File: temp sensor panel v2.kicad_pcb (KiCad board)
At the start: 2 copper layers, 48.2 x 24.9 mm, 51 parts, among them IC1 ESP32-C3-MINI-1, J1 USB_C_Receptacle_USB2.0, J2 Conn_01x02_Male, J3 Conn_01x06_Male, J4 USB_B_Micro, J5 Conn_01x02_Male, J6 Conn_01x02_Male, Q1 BC847BDW1, SW1 SW_Push_Right_Angle, SW2 SW_Push_Right_Angle, U1 SHTC3, U2 TLV62569DBV, U3 BME280, U4 Si7020-A20, U5 SN65220

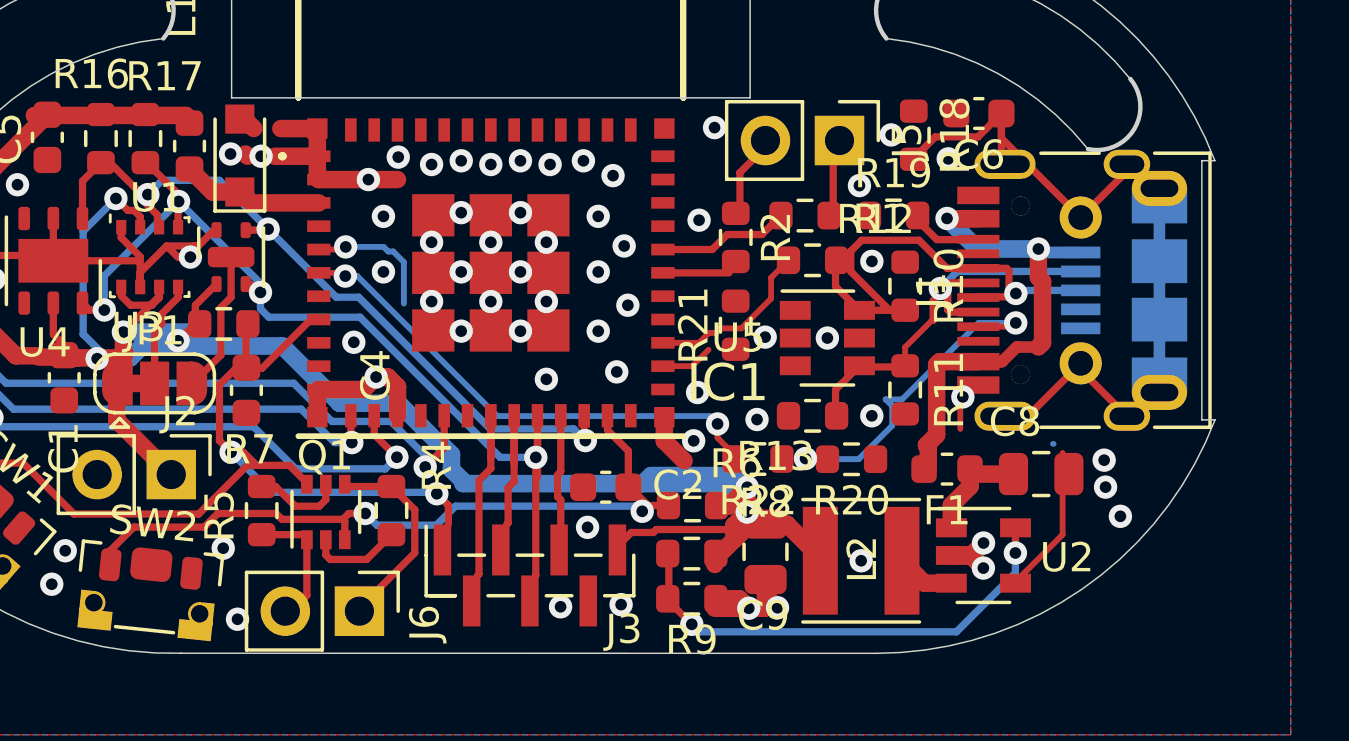
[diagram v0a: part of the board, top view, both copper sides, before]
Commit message: added fuse and some layout changes
Signed-off-by: lokimetasmith <lokimail@gmail.com>
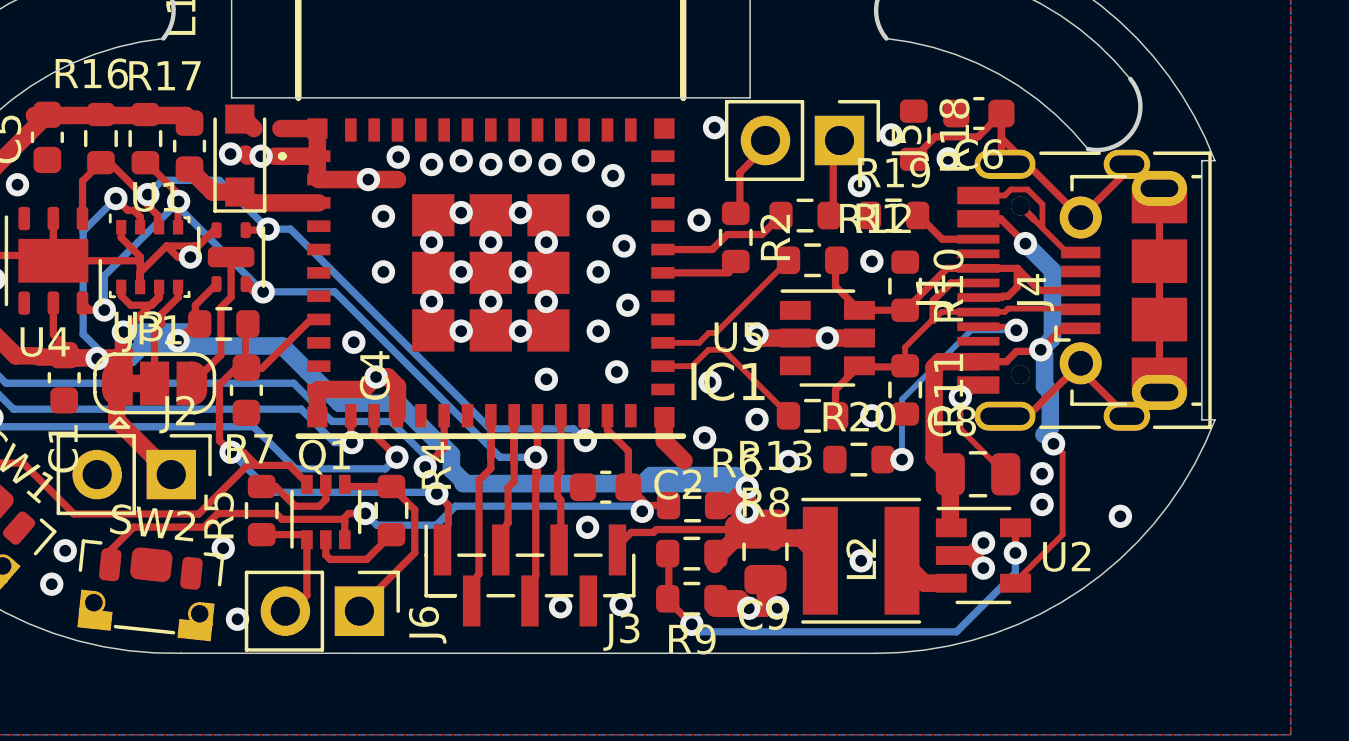
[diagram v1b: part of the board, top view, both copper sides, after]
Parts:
- removed F1: 6V 0.5A, Fuse:Fuse_0603_1608Metric
- removed R21, R22: 5.1k, Resistor_SMD:R_0603_1608Metric
- J4: moved to F.Cu
- moved C8 2.17 mm to (157.0, 99.0)
- moved R20 0.25 mm to (153.0, 98.5), turned to 0 degrees
- turned J4 to 90 degrees
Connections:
- net /CC1 renamed Net-(J1-PadA5)
- net /CC2 renamed Net-(J1-PadB5)
- IC1 pad 5: /I37_pico -> (no net)
- IC1 pad 6: /I38_pico -> (no net)
- J1 pad : (no net) -> GND
- J1 pad A4: /V_USB -> +5V
- J1 pad A9: /V_USB -> +5V
- J1 pad B4: /V_USB -> +5V
- J1 pad B9: /V_USB -> +5V
- J4 pad 1: /V_USB -> +5V
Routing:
- net +5V: track 9.04 -> 26.7 mm, vias 0 -> 3
- net /I38_pico: track 17.3 -> 0.00 mm, vias 2 -> 0
- net /V_USB: track 17.1 -> 0.00 mm, vias 2 -> 0
- net GND: track 45.5 -> 57.4 mm, vias 67 -> 69
- net /D+: track 17.3 -> 12.7 mm, vias 1 -> 0
- net /I37_pico: track 4.59 -> 0.00 mm, vias 1 -> 0
- net /IO20_pico: track 1.80 -> 5.52 mm
- net Net-(J1-PadA5): track 11.2 -> 8.97 mm, vias 3 -> 2
- net /D-: track 15.2 -> 13.4 mm, vias 1 -> 0

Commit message: initial work on gerber files, there's an error where arches aren't rendered correctly
Signed-off-by: lokimetasmith <lokimail@gmail.com>
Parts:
- removed the C8 at (157.0, 99.0)
- removed the JP1 at (128.8, 95.8)
- removed the R10 at (154.5, 92.5)
- removed the R11 at (154.5, 96.1)
- removed the R12 at (151.4, 91.6)
- removed the R13 at (151.4, 97.0)
- removed the R20 at (153.0, 98.5)
- removed the U5 at (151.9, 94.3)
- added C1: 0.1u, Capacitor_SMD:C_0603_1608Metric, F.Cu at (33.6, 182.6)
- added C1: 0.1u, Capacitor_SMD:C_0603_1608Metric, F.Cu at (63.2, 148.3)
- added C1: 0.1u, Capacitor_SMD:C_0603_1608Metric, F.Cu at (120.8, 148.3)
- added C1: 0.1u, Capacitor_SMD:C_0603_1608Metric, F.Cu at (91.2, 182.6)
- added C2: 0.1u, Capacitor_SMD:C_0603_1608Metric, F.Cu at (44.7, 144.6)
- added C2: 0.1u, Capacitor_SMD:C_0603_1608Metric, F.Cu at (52.2, 186.4)
- added C2: 0.1u, Capacitor_SMD:C_0603_1608Metric, F.Cu at (102.2, 144.6)
- added C2: 0.1u, Capacitor_SMD:C_0603_1608Metric, F.Cu at (109.8, 186.4)
- added C3: 10u, Capacitor_SMD:C_0805_2012Metric, F.Cu at (30.4, 177.5)
- added C3: 10u, Capacitor_SMD:C_0805_2012Metric, F.Cu at (66.5, 153.4)
- added C3: 10u, Capacitor_SMD:C_0805_2012Metric, F.Cu at (124.0, 153.4)
- added C3: 10u, Capacitor_SMD:C_0805_2012Metric, F.Cu at (88.0, 177.5)
- added C4: 0.1u, Capacitor_SMD:C_0603_1608Metric, F.Cu at (57.0, 147.9)
- added C4: 0.1u, Capacitor_SMD:C_0603_1608Metric, F.Cu at (39.9, 183.1)
- added C4: 0.1u, Capacitor_SMD:C_0603_1608Metric, F.Cu at (114.5, 147.9)
- added C4: 0.1u, Capacitor_SMD:C_0603_1608Metric, F.Cu at (97.5, 183.1)
- added C5: 0.1u, Capacitor_SMD:C_0603_1608Metric, F.Cu at (63.8, 156.6)
- added C5: 0.1u, Capacitor_SMD:C_0603_1608Metric, F.Cu at (33.1, 174.4)
- added C5: 0.1u, Capacitor_SMD:C_0603_1608Metric, F.Cu at (121.4, 156.6)
- added C5: 0.1u, Capacitor_SMD:C_0603_1608Metric, F.Cu at (90.6, 174.4)
- added C6: 0.01u, Capacitor_SMD:C_0603_1608Metric, F.Cu at (31.9, 157.4)
- added C6: 0.01u, Capacitor_SMD:C_0603_1608Metric, F.Cu at (65.0, 173.6)
- added C6: 0.01u, Capacitor_SMD:C_0603_1608Metric, F.Cu at (89.4, 157.4)
- added C6: 0.01u, Capacitor_SMD:C_0603_1608Metric, F.Cu at (122.6, 173.6)
- added C8: 4.7u, Capacitor_SMD:C_0805_2012Metric, F.Cu at (29.7, 145.0)
- added C8: 4.7u, Capacitor_SMD:C_0805_2012Metric, F.Cu at (67.1, 185.9)
- added C8: 4.7u, Capacitor_SMD:C_0805_2012Metric, F.Cu at (87.3, 145.0)
- added C8: 4.7u, Capacitor_SMD:C_0805_2012Metric, F.Cu at (124.7, 185.9)
- added C8: 4.7u, Capacitor_SMD:C_0805_2012Metric, F.Cu at (159.2, 98.9)
- added C9: 10u, Capacitor_SMD:C_0805_2012Metric, F.Cu at (57.7, 188.6)
- added C9: 10u, Capacitor_SMD:C_0805_2012Metric, F.Cu at (39.2, 142.3)
- added C9: 10u, Capacitor_SMD:C_0805_2012Metric, F.Cu at (96.7, 142.3)
- added C9: 10u, Capacitor_SMD:C_0805_2012Metric, F.Cu at (115.3, 188.6)
- added D1: 3.3v_TVS, Diode_SMD:D_SOD-323_HandSoldering, F.Cu at (39.7, 175.0)
- added D1: 3.3v_TVS, Diode_SMD:D_SOD-323_HandSoldering, F.Cu at (57.2, 155.9)
- added D1: 3.3v_TVS, Diode_SMD:D_SOD-323_HandSoldering, F.Cu at (114.8, 155.9)
- added D1: 3.3v_TVS, Diode_SMD:D_SOD-323_HandSoldering, F.Cu at (97.2, 175.0)
- added D2: QLS6A, LED_SMD:LED_Cree-PLCC6_4.7x1.5mm, F.Cu at (26.2, 179.6)
- added D2: QLS6A, LED_SMD:LED_Cree-PLCC6_4.7x1.5mm, F.Cu at (70.7, 151.3)
- added D2: QLS6A, LED_SMD:LED_Cree-PLCC6_4.7x1.5mm, F.Cu at (128.3, 151.3)
- added D2: QLS6A, LED_SMD:LED_Cree-PLCC6_4.7x1.5mm, F.Cu at (83.7, 179.6)
- added F1: 6V 0.5A, Fuse:Fuse_0603_1608Metric, F.Cu at (63.9, 185.8)
- added F1: 6V 0.5A, Fuse:Fuse_0603_1608Metric, F.Cu at (33.0, 145.2)
- added F1: 6V 0.5A, Fuse:Fuse_0603_1608Metric, F.Cu at (90.5, 145.2)
- added F1: 6V 0.5A, Fuse:Fuse_0603_1608Metric, F.Cu at (121.5, 185.8)
- added F1: 6V 0.5A, Fuse:Fuse_0603_1608Metric, F.Cu at (156.0, 98.8)
- added IC1: ESP32-C3-MINI-1, Twig:ESP32C3MINI1, F.Cu at (48.6, 154.6)
- added IC1: ESP32-C3-MINI-1, Twig:ESP32C3MINI1, F.Cu at (48.3, 176.3)
- added IC1: ESP32-C3-MINI-1, Twig:ESP32C3MINI1, F.Cu at (106.2, 154.6)
- added IC1: ESP32-C3-MINI-1, Twig:ESP32C3MINI1, F.Cu at (105.8, 176.3)
- added J1: USB_C_Receptacle_USB2.0, Connector_USB:USB_C_Receptacle_HRO_TYPE-C-31-M-12, F.Cu at (27.8, 151.3)
- added J1: USB_C_Receptacle_USB2.0, Connector_USB:USB_C_Receptacle_HRO_TYPE-C-31-M-12, F.Cu at (69.0, 179.6)
- added J1: USB_C_Receptacle_USB2.0, Connector_USB:USB_C_Receptacle_HRO_TYPE-C-31-M-12, F.Cu at (85.4, 151.3)
- added J1: USB_C_Receptacle_USB2.0, Connector_USB:USB_C_Receptacle_HRO_TYPE-C-31-M-12, F.Cu at (126.6, 179.6)
- added J2: Conn_01x02_Male, Connector_PinHeader_2.54mm:PinHeader_1x02_P2.54mm_Vertical, F.Cu at (37.3, 186.0)
- added J2: Conn_01x02_Male, Connector_PinHeader_2.54mm:PinHeader_1x02_P2.54mm_Vertical, F.Cu at (59.6, 145.0)
- added J2: Conn_01x02_Male, Connector_PinHeader_2.54mm:PinHeader_1x02_P2.54mm_Vertical, F.Cu at (117.1, 145.0)
- added J2: Conn_01x02_Male, Connector_PinHeader_2.54mm:PinHeader_1x02_P2.54mm_Vertical, F.Cu at (94.9, 186.0)
- added J3: Conn_01x06_Male, Connector_PinHeader_1.00mm:PinHeader_1x07_P1.00mm_Vertical_SMD_Pin1Right, F.Cu at (47.3, 141.5)
- added J3: Conn_01x06_Male, Connector_PinHeader_1.00mm:PinHeader_1x07_P1.00mm_Vertical_SMD_Pin1Right, F.Cu at (49.6, 189.4)
- added J3: Conn_01x06_Male, Connector_PinHeader_1.00mm:PinHeader_1x07_P1.00mm_Vertical_SMD_Pin1Right, F.Cu at (104.8, 141.5)
- added J3: Conn_01x06_Male, Connector_PinHeader_1.00mm:PinHeader_1x07_P1.00mm_Vertical_SMD_Pin1Right, F.Cu at (107.2, 189.4)
- added J4: USB_B_Micro, Connector_USB:USB_Micro-B_Molex-105017-0001, B.Cu at (26.9, 151.3)
- added J4: USB_B_Micro, Connector_USB:USB_Micro-B_Molex-105017-0001, B.Cu at (70.0, 179.6)
- added J4: USB_B_Micro, Connector_USB:USB_Micro-B_Molex-105017-0001, B.Cu at (84.5, 151.3)
- added J4: USB_B_Micro, Connector_USB:USB_Micro-B_Molex-105017-0001, B.Cu at (127.5, 179.6)
- added J5: Conn_01x02_Male, Connector_PinHeader_2.54mm:PinHeader_1x02_P2.54mm_Vertical, F.Cu at (36.6, 156.4)
- added J5: Conn_01x02_Male, Connector_PinHeader_2.54mm:PinHeader_1x02_P2.54mm_Vertical, F.Cu at (60.2, 174.5)
- added J5: Conn_01x02_Male, Connector_PinHeader_2.54mm:PinHeader_1x02_P2.54mm_Vertical, F.Cu at (94.2, 156.4)
- added J5: Conn_01x02_Male, Connector_PinHeader_2.54mm:PinHeader_1x02_P2.54mm_Vertical, F.Cu at (117.8, 174.5)
- added J6: Conn_01x02_Male, Connector_PinHeader_2.54mm:PinHeader_1x02_P2.54mm_Vertical, F.Cu at (53.1, 140.3)
- added J6: Conn_01x02_Male, Connector_PinHeader_2.54mm:PinHeader_1x02_P2.54mm_Vertical, F.Cu at (43.8, 190.6)
- added J6: Conn_01x02_Male, Connector_PinHeader_2.54mm:PinHeader_1x02_P2.54mm_Vertical, F.Cu at (110.7, 140.3)
- added J6: Conn_01x02_Male, Connector_PinHeader_2.54mm:PinHeader_1x02_P2.54mm_Vertical, F.Cu at (101.3, 190.6)
- added JP1: Jumper_3_Bridged12, Twig:Jumper_0603_1608Metric, F.Cu at (36.0, 182.8)
- added JP1: Jumper_3_Bridged12, Twig:Jumper_0603_1608Metric, F.Cu at (60.9, 148.1)
- added JP1: Jumper_3_Bridged12, Twig:Jumper_0603_1608Metric, F.Cu at (118.5, 148.1)
- added JP1: Jumper_3_Bridged12, Twig:Jumper_0603_1608Metric, F.Cu at (93.5, 182.8)
- added JP1: Jumper_3_Bridged12, Twig:Jumper_0603_1608Metric, F.Cu at (128.0, 95.8)
- added L1: L_Core_Ferrite_Small, Inductor_SMD:L_0603_1608Metric, F.Cu at (58.9, 156.2)
- added L1: L_Core_Ferrite_Small, Inductor_SMD:L_0603_1608Metric, F.Cu at (37.9, 174.7)
- added L1: L_Core_Ferrite_Small, Inductor_SMD:L_0603_1608Metric, F.Cu at (116.5, 156.2)
- added L1: L_Core_Ferrite_Small, Inductor_SMD:L_0603_1608Metric, F.Cu at (95.5, 174.7)
- added L2: 2.2uH, Inductor_SMD:L_Taiyo-Yuden_MD-4040, F.Cu at (35.9, 142.0)
- added L2: 2.2uH, Inductor_SMD:L_Taiyo-Yuden_MD-4040, F.Cu at (61.0, 188.9)
- added L2: 2.2uH, Inductor_SMD:L_Taiyo-Yuden_MD-4040, F.Cu at (93.5, 142.0)
- added L2: 2.2uH, Inductor_SMD:L_Taiyo-Yuden_MD-4040, F.Cu at (118.5, 188.9)
- added Q1: BC847BDW1, Package_TO_SOT_SMD:SOT-363_SC-70-6, F.Cu at (42.6, 187.2)
- added Q1: BC847BDW1, Package_TO_SOT_SMD:SOT-363_SC-70-6, F.Cu at (54.3, 143.7)
- added Q1: BC847BDW1, Package_TO_SOT_SMD:SOT-363_SC-70-6, F.Cu at (111.8, 143.7)
- added Q1: BC847BDW1, Package_TO_SOT_SMD:SOT-363_SC-70-6, F.Cu at (100.2, 187.2)
- added R1: 499R, Resistor_SMD:R_0603_1608Metric, F.Cu at (59.0, 177.1)
- added R1: 499R, Resistor_SMD:R_0603_1608Metric, F.Cu at (37.8, 153.9)
- added R1: 499R, Resistor_SMD:R_0603_1608Metric, F.Cu at (95.4, 153.9)
- added R1: 499R, Resistor_SMD:R_0603_1608Metric, F.Cu at (116.6, 177.1)
- added R10: 15K, Resistor_SMD:R_0603_1608Metric, F.Cu at (36.3, 152.4)
- added R10: 15K, Resistor_SMD:R_0603_1608Metric, F.Cu at (60.5, 178.6)
- added R10: 15K, Resistor_SMD:R_0603_1608Metric, F.Cu at (93.9, 152.4)
- added R10: 15K, Resistor_SMD:R_0603_1608Metric, F.Cu at (118.1, 178.6)
- added R10: 15K, Resistor_SMD:R_0603_1608Metric, F.Cu at (152.6, 91.6)
- added R11: 15K, Resistor_SMD:R_0603_1608Metric, F.Cu at (60.4, 183.7)
- added R11: 15K, Resistor_SMD:R_0603_1608Metric, F.Cu at (36.4, 147.3)
- added R11: 15K, Resistor_SMD:R_0603_1608Metric, F.Cu at (94.0, 147.3)
- added R11: 15K, Resistor_SMD:R_0603_1608Metric, F.Cu at (118.0, 183.7)
- added R11: 15K, Resistor_SMD:R_0603_1608Metric, F.Cu at (152.5, 96.7)
- added R12: 27, Resistor_SMD:R_0603_1608Metric, F.Cu at (57.4, 180.8)
- added R12: 27, Resistor_SMD:R_0603_1608Metric, F.Cu at (39.4, 150.2)
- added R12: 27, Resistor_SMD:R_0603_1608Metric, F.Cu at (97.0, 150.2)
- added R12: 27, Resistor_SMD:R_0603_1608Metric, F.Cu at (115.0, 180.8)
- added R12: 27, Resistor_SMD:R_0603_1608Metric, F.Cu at (149.5, 93.8)
- added R13: 27, Resistor_SMD:R_0603_1608Metric, F.Cu at (39.4, 148.4)
- added R13: 27, Resistor_SMD:R_0603_1608Metric, F.Cu at (57.4, 182.6)
- added R13: 27, Resistor_SMD:R_0603_1608Metric, F.Cu at (97.0, 148.4)
- added R13: 27, Resistor_SMD:R_0603_1608Metric, F.Cu at (115.0, 182.6)
- added R13: 27, Resistor_SMD:R_0603_1608Metric, F.Cu at (149.5, 95.6)
- added R14: 100, Resistor_SMD:R_0603_1608Metric, F.Cu at (28.9, 183.2)
- added R14: 100, Resistor_SMD:R_0603_1608Metric, F.Cu at (68.0, 147.8)
- added R14: 100, Resistor_SMD:R_0603_1608Metric, F.Cu at (125.5, 147.8)
- added R14: 100, Resistor_SMD:R_0603_1608Metric, F.Cu at (86.5, 183.2)
- added R15: 100, Resistor_SMD:R_0603_1608Metric, F.Cu at (28.2, 177.9)
- added R15: 100, Resistor_SMD:R_0603_1608Metric, F.Cu at (68.7, 153.1)
- added R15: 100, Resistor_SMD:R_0603_1608Metric, F.Cu at (126.3, 153.1)
- added R15: 100, Resistor_SMD:R_0603_1608Metric, F.Cu at (85.7, 177.9)
- added R16: 10K, Resistor_SMD:R_0603_1608Metric, F.Cu at (62.0, 156.5)
- added R16: 10K, Resistor_SMD:R_0603_1608Metric, F.Cu at (34.9, 174.4)
- added R16: 10K, Resistor_SMD:R_0603_1608Metric, F.Cu at (119.5, 156.5)
- added R16: 10K, Resistor_SMD:R_0603_1608Metric, F.Cu at (92.5, 174.4)
- added R17: 10K, Resistor_SMD:R_0603_1608Metric, F.Cu at (36.4, 174.4)
- added R17: 10K, Resistor_SMD:R_0603_1608Metric, F.Cu at (60.4, 156.5)
- added R17: 10K, Resistor_SMD:R_0603_1608Metric, F.Cu at (118.0, 156.5)
- added R17: 10K, Resistor_SMD:R_0603_1608Metric, F.Cu at (94.0, 174.4)
- added R18: 680k, Resistor_SMD:R_0603_1608Metric, F.Cu at (34.1, 156.6)
- added R18: 680k, Resistor_SMD:R_0603_1608Metric, F.Cu at (62.8, 174.3)
- added R18: 680k, Resistor_SMD:R_0603_1608Metric, F.Cu at (91.7, 156.6)
- added R18: 680k, Resistor_SMD:R_0603_1608Metric, F.Cu at (120.3, 174.3)
- added R19: 5.1k, Resistor_SMD:R_0603_1608Metric, F.Cu at (34.8, 153.9)
- added R19: 5.1k, Resistor_SMD:R_0603_1608Metric, F.Cu at (62.1, 177.1)
- added R19: 5.1k, Resistor_SMD:R_0603_1608Metric, F.Cu at (92.4, 153.9)
- added R19: 5.1k, Resistor_SMD:R_0603_1608Metric, F.Cu at (119.6, 177.1)
- added R2: 499R, Resistor_SMD:R_0603_1608Metric, F.Cu at (56.7, 177.8)
- added R2: 499R, Resistor_SMD:R_0603_1608Metric, F.Cu at (40.2, 153.1)
- added R2: 499R, Resistor_SMD:R_0603_1608Metric, F.Cu at (97.8, 153.1)
- added R2: 499R, Resistor_SMD:R_0603_1608Metric, F.Cu at (114.2, 177.8)
- added R20: 5.1k, Resistor_SMD:R_0603_1608Metric, F.Cu at (36.3, 145.8)
- added R20: 5.1k, Resistor_SMD:R_0603_1608Metric, F.Cu at (60.6, 185.2)
- added R20: 5.1k, Resistor_SMD:R_0603_1608Metric, F.Cu at (93.8, 145.8)
- added R20: 5.1k, Resistor_SMD:R_0603_1608Metric, F.Cu at (118.2, 185.2)
- added R20: 5.1k, Resistor_SMD:R_0603_1608Metric, F.Cu at (152.7, 98.2)
- added R3: 200, Resistor_SMD:R_0603_1608Metric, F.Cu at (28.2, 180.9)
- added R3: 200, Resistor_SMD:R_0603_1608Metric, F.Cu at (68.7, 150.1)
- added R3: 200, Resistor_SMD:R_0603_1608Metric, F.Cu at (126.3, 150.1)
- added R3: 200, Resistor_SMD:R_0603_1608Metric, F.Cu at (85.7, 180.9)
- added R4: 10K, Resistor_SMD:R_0603_1608Metric, F.Cu at (44.9, 187.2)
- added R4: 10K, Resistor_SMD:R_0603_1608Metric, F.Cu at (52.0, 143.8)
- added R4: 10K, Resistor_SMD:R_0603_1608Metric, F.Cu at (109.6, 143.8)
- added R4: 10K, Resistor_SMD:R_0603_1608Metric, F.Cu at (102.4, 187.2)
- added R5: 10K, Resistor_SMD:R_0603_1608Metric, F.Cu at (56.5, 143.8)
- added R5: 10K, Resistor_SMD:R_0603_1608Metric, F.Cu at (40.4, 187.2)
- added R5: 10K, Resistor_SMD:R_0603_1608Metric, F.Cu at (114.0, 143.8)
- added R5: 10K, Resistor_SMD:R_0603_1608Metric, F.Cu at (98.0, 187.2)
- added R6: 10K, Resistor_SMD:R_0603_1608Metric, F.Cu at (55.2, 187.0)
- added R6: 10K, Resistor_SMD:R_0603_1608Metric, F.Cu at (41.7, 143.9)
- added R6: 10K, Resistor_SMD:R_0603_1608Metric, F.Cu at (99.2, 143.9)
- added R6: 10K, Resistor_SMD:R_0603_1608Metric, F.Cu at (112.8, 187.0)
- added R7: 10K, Resistor_SMD:R_0603_1608Metric, F.Cu at (39.1, 180.8)
- added R7: 10K, Resistor_SMD:R_0603_1608Metric, F.Cu at (57.8, 150.2)
- added R7: 10K, Resistor_SMD:R_0603_1608Metric, F.Cu at (115.3, 150.2)
- added R7: 10K, Resistor_SMD:R_0603_1608Metric, F.Cu at (96.7, 180.8)
- added R8: 680k, Resistor_SMD:R_0603_1608Metric, F.Cu at (41.7, 142.3)
- added R8: 680k, Resistor_SMD:R_0603_1608Metric, F.Cu at (55.2, 188.7)
- added R8: 680k, Resistor_SMD:R_0603_1608Metric, F.Cu at (99.3, 142.3)
- added R8: 680k, Resistor_SMD:R_0603_1608Metric, F.Cu at (112.7, 188.7)
- added R9: 150K, Resistor_SMD:R_0603_1608Metric, F.Cu at (55.2, 190.2)
- added R9: 150K, Resistor_SMD:R_0603_1608Metric, F.Cu at (41.7, 140.7)
- added R9: 150K, Resistor_SMD:R_0603_1608Metric, F.Cu at (99.3, 140.7)
- added R9: 150K, Resistor_SMD:R_0603_1608Metric, F.Cu at (112.7, 190.2)
- added REF**: VAL**, Twig:z_Drill_05x10, F.Cu at (84.9, 201.8)
- added REF**: DOUBLE_SIDED_TAB, mte_panelizing:DOUBLE_SIDED_TAB, F.Cu at (106.1, 158.9)
- added REF**: DOUBLE_SIDED_TAB, mte_panelizing:DOUBLE_SIDED_TAB, F.Cu at (105.9, 172.0)
- added REF**: DOUBLE_SIDED_TAB, mte_panelizing:DOUBLE_SIDED_TAB, F.Cu at (131.3, 179.6)
- added REF**: DOUBLE_SIDED_TAB, mte_panelizing:DOUBLE_SIDED_TAB, F.Cu at (165.8, 92.6)
- added REF**: DOUBLE_SIDED_TAB, mte_panelizing:DOUBLE_SIDED_TAB, F.Cu at (140.4, 85.0)
- added REF**: SINGLE_SIDED_TAB, mte_panelizing:SINGLE_SIDED_TAB, F.Cu at (107.8, 193.1)
- added REF**: DOUBLE_SIDED_TAB, mte_panelizing:DOUBLE_SIDED_TAB, F.Cu at (82.6, 96.1)
- added REF**: VAL**, Twig:z_Drill_05x10, F.Cu at (58.6, 115.9)
- added REF**: SINGLE_SIDED_TAB, mte_panelizing:SINGLE_SIDED_TAB, F.Cu at (44.9, 137.8)
- added REF**: SINGLE_SIDED_TAB, mte_panelizing:SINGLE_SIDED_TAB, F.Cu at (104.2, 137.8)
- added REF**: DOUBLE_SIDED_TAB, mte_panelizing:DOUBLE_SIDED_TAB, F.Cu at (73.7, 179.6)
- added REF**: DOUBLE_SIDED_TAB, mte_panelizing:DOUBLE_SIDED_TAB, F.Cu at (48.3, 172.0)
- added REF**: SINGLE_SIDED_TAB, mte_panelizing:SINGLE_SIDED_TAB, F.Cu at (50.2, 193.1)
- added REF**: DOUBLE_SIDED_TAB, mte_panelizing:DOUBLE_SIDED_TAB, F.Cu at (23.1, 151.3)
- added REF**: DOUBLE_SIDED_TAB, mte_panelizing:DOUBLE_SIDED_TAB, F.Cu at (48.3, 158.9)
- added REF**: DOUBLE_SIDED_TAB, mte_panelizing:DOUBLE_SIDED_TAB, F.Cu at (80.7, 151.3)
- added REF_stackup: FabDrawing-4Layer, Twig:FabDrawing-2Layer-Metric, F.Cu at (53.6, 19.6)
- added Ref**: Val**, Twig:simplified logo_plain_svg, F.Cu at (44.9, 149.3)
- added Ref**: Val**, Twig:simplified logo_plain_svg, F.Cu at (51.9, 181.6)
- added Ref**: Val**, Twig:simplified logo_plain_svg, F.Cu at (102.5, 149.3)
- added Ref**: Val**, Twig:simplified logo_plain_svg, F.Cu at (109.5, 181.6)
- added Ref**: Val**, Twig:simplified logo_plain_svg, F.Cu at (144.0, 94.6)
- added SW1: SW_Push_Right_Angle, Twig:SW_Push_1P1T-MP_NO_Horizontal_TL6340, F.Cu at (66.5, 143.3)
- added SW1: SW_Push_Right_Angle, Twig:SW_Push_1P1T-MP_NO_Horizontal_TL6340, F.Cu at (30.4, 187.6)
- added SW1: SW_Push_Right_Angle, Twig:SW_Push_1P1T-MP_NO_Horizontal_TL6340, F.Cu at (124.0, 143.3)
- added SW1: SW_Push_Right_Angle, Twig:SW_Push_1P1T-MP_NO_Horizontal_TL6340, F.Cu at (88.0, 187.6)
- added SW2: SW_Push_Right_Angle, Twig:SW_Push_1P1T-MP_NO_Horizontal_TL6340, F.Cu at (60.4, 140.8)
- added SW2: SW_Push_Right_Angle, Twig:SW_Push_1P1T-MP_NO_Horizontal_TL6340, F.Cu at (36.5, 190.1)
- added SW2: SW_Push_Right_Angle, Twig:SW_Push_1P1T-MP_NO_Horizontal_TL6340, F.Cu at (117.9, 140.8)
- added SW2: SW_Push_Right_Angle, Twig:SW_Push_1P1T-MP_NO_Horizontal_TL6340, F.Cu at (94.1, 190.1)
- added U1: SHTC3, Sensor_Humidity:Sensirion_DFN-4-1EP_2x2mm_P1mm_EP0.7x1.6mm, F.Cu at (57.5, 152.4)
- added U1: SHTC3, Sensor_Humidity:Sensirion_DFN-4-1EP_2x2mm_P1mm_EP0.7x1.6mm, F.Cu at (39.4, 178.5)
- added U1: SHTC3, Sensor_Humidity:Sensirion_DFN-4-1EP_2x2mm_P1mm_EP0.7x1.6mm, F.Cu at (115.1, 152.4)
- added U1: SHTC3, Sensor_Humidity:Sensirion_DFN-4-1EP_2x2mm_P1mm_EP0.7x1.6mm, F.Cu at (96.9, 178.5)
- added U2: TLV62569DBV, Package_TO_SOT_SMD:SOT-23-5, F.Cu at (65.2, 188.7)
- added U2: TLV62569DBV, Package_TO_SOT_SMD:SOT-23-5, F.Cu at (31.7, 142.2)
- added U2: TLV62569DBV, Package_TO_SOT_SMD:SOT-23-5, F.Cu at (89.3, 142.2)
- added U2: TLV62569DBV, Package_TO_SOT_SMD:SOT-23-5, F.Cu at (122.7, 188.7)
- added U3: BME280, Package_LGA:Bosch_LGA-8_2.5x2.5mm_P0.65mm_ClockwisePinNumbering, F.Cu at (60.3, 152.4)
- added U3: BME280, Package_LGA:Bosch_LGA-8_2.5x2.5mm_P0.65mm_ClockwisePinNumbering, F.Cu at (36.6, 178.5)
- added U3: BME280, Package_LGA:Bosch_LGA-8_2.5x2.5mm_P0.65mm_ClockwisePinNumbering, F.Cu at (117.9, 152.4)
- added U3: BME280, Package_LGA:Bosch_LGA-8_2.5x2.5mm_P0.65mm_ClockwisePinNumbering, F.Cu at (94.1, 178.5)
- added U4: Si7020-A20, Package_DFN_QFN:DFN-6-1EP_3x3mm_P1mm_EP1.5x2.4mm, F.Cu at (33.3, 178.6)
- added U4: Si7020-A20, Package_DFN_QFN:DFN-6-1EP_3x3mm_P1mm_EP1.5x2.4mm, F.Cu at (63.6, 152.3)
- added U4: Si7020-A20, Package_DFN_QFN:DFN-6-1EP_3x3mm_P1mm_EP1.5x2.4mm, F.Cu at (121.2, 152.3)
- added U4: Si7020-A20, Package_DFN_QFN:DFN-6-1EP_3x3mm_P1mm_EP1.5x2.4mm, F.Cu at (90.8, 178.6)
- added U5: SN65220, Package_TO_SOT_SMD:SOT-23-6, F.Cu at (36.0, 149.8)
- added U5: SN65220, Package_TO_SOT_SMD:SOT-23-6, F.Cu at (60.8, 181.1)
- added U5: SN65220, Package_TO_SOT_SMD:SOT-23-6, F.Cu at (93.6, 149.8)
- added U5: SN65220, Package_TO_SOT_SMD:SOT-23-6, F.Cu at (118.4, 181.1)
- added U5: SN65220, Package_TO_SOT_SMD:SOT-23-6, F.Cu at (152.9, 94.1)
- J4: moved to B.Cu
- turned J4 to 270 degrees
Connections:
- net Net-(J1-PadB5) renamed /CC2
- IC1 pad 26: /IO20_pico -> /USB_D-
- IC1 pad 27: /IO7_pico -> /USB_D+
- J1 pad : GND -> (no net)
- J1 pad A4: +5V -> /V_USB
- J1 pad A5: Net-(J1-PadA5) -> /CC1
- J1 pad A9: +5V -> /V_USB
- J1 pad B4: +5V -> /V_USB
- J1 pad B9: +5V -> /V_USB
- J4 pad 1: +5V -> /V_USB
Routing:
- net +3V3: track 104.5 -> 560.4 mm, vias 6 -> 30
- net GND: track 57.4 -> 335.7 mm, vias 69 -> 365
- net /EN: track 32.1 -> 176.9 mm, vias 2 -> 10
- net /Shield: track 27.8 -> 171.4 mm
- net /IO13_pico: track 32.8 -> 161.3 mm, vias 4 -> 20
- net /IO2_pico: track 26.7 -> 138.0 mm, vias 3 -> 15
- net /V_USB: track 0.00 -> 108.6 mm, vias 0 -> 10
- net /Boot_Option: track 25.3 -> 125.0 mm, vias 2 -> 10
- net /IO32_pico: track 22.2 -> 110.5 mm, vias 2 -> 10
- net /IO26_pico: track 21.8 -> 103.0 mm, vias 2 -> 10
- net /D+: track 12.7 -> 82.7 mm, vias 0 -> 5
- net /IO33_pico: track 18.4 -> 86.2 mm, vias 2 -> 10
- net Net-(R8-Pad1): track 15.8 -> 80.3 mm, vias 2 -> 10
- net /D-: track 13.4 -> 77.0 mm, vias 0 -> 5
- net /CC1: track 0.00 -> 58.9 mm, vias 0 -> 10
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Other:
- board size 48.2 x 24.9 mm -> 145.2 x 114.8 mm
- net class USB_Data added: clearance 0.1524, trace_width 0.1524, via_dia 0.6858, via_drill 0.3302
- rule pad_to_mask_clearance: 0.05 -> 0
- rule trace_min: 0.2 -> 0.1524
- rule via_min_drill: 0.3 -> 0.254
- rule via_min_size: 0.4 -> 0.508
- board text added: "BOOT"
- board text added: "JuniperTechnology.co"
- board text added: "RST"
- board text added: "V0.2"
